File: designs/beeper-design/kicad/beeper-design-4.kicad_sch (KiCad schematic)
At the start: 37 parts, among them J1 TC2030-IDC-NL, J6 10103594-0001LF, U1 DA14705-00000HZ2, U2 AT25FF321A-UUN-T, U7 TPD4S012DRYR

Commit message: another export
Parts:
- removed C1: 22u, beeper-design:Pkg0603, symbol C86295
- removed C10: 2.2u, beeper-design:Pkg0201_37, symbol C335106_24
- removed C11: 2.2u, beeper-design:Pkg0201_29, symbol C335106_19
- removed C12: 2.2u, beeper-design:Pkg0201_48, symbol C335106_30
- removed C13: 2.2u, beeper-design:Pkg0201_51, symbol C335106_33
- removed C2: 22u, beeper-design:Pkg0603_1, symbol C86295_1
- removed C3: 22u, beeper-design:Pkg0603_2, symbol C86295_2
- removed C36: 2.2u, beeper-design:Pkg0201_49, symbol C335106_31
- removed C4: 47u, beeper-design:Pkg0805, symbol my_capacitor
- removed C49: 2.2u, beeper-design:Pkg0201_4, symbol C335106_1
- removed C5: 2.2u, beeper-design:Pkg0201_24, symbol C335106_14
- removed C50: 2.2u, beeper-design:Pkg0201_25, symbol C335106_15
- removed C6: 47u, beeper-design:Pkg0805_1, symbol my_capacitor_1
- removed C7: 2.2u, beeper-design:Pkg0201_50, symbol C335106_32
- removed C8: 2.2u, beeper-design:Pkg0201_6, symbol C335106_2
- removed C9: 2.2u, beeper-design:Pkg0201_22, symbol C335106_12
- removed J1: TC2030-IDC-NL, beeper-design:TC2030_IDC_NL_FOOTPRINT, symbol component_1
- removed J6: 10103594-0001LF, beeper-design:AMPHENOL_10103594_0001LF, symbol AMPHENOL_10103594_0001LF
- removed L1: 470n, beeper-design:Pkg0201_1, symbol my_inductor_3
- removed L2: 470n, beeper-design:Pkg0201_14, symbol my_inductor_1
- removed L3: 470n, beeper-design:Pkg0201_13, symbol my_inductor
- removed L4: 470n, beeper-design:Pkg0201_36, symbol my_inductor_2
- removed R1: 0R, beeper-design:Pkg0201_44, symbol my_resistor_11
- removed R18: 100K, beeper-design:Pkg0201_38, symbol my_resistor_8
- removed TP10, TP11, TP12, TP5, TP6, TP7, TP8, TP9: (no value), beeper-design:SMD_TESTPT, symbol smd_testpoint_cmp
- removed U1: DA14705-00000HZ2, beeper-design:LP, symbol DA14705
- removed U17: (no value), beeper-design:Pkg_2450AT18D0100_STD_R_1, symbol Sym2450AT18D0100001E
- removed U2: AT25FF321A-UUN-T, beeper-design:WLCSP_12, symbol AT25FF321A_UUN_T
- removed U7: TPD4S012DRYR, beeper-design:SON_6_L1_5_W1_0_P0_50_BL, symbol C96506
- removed XTAL1: XRCGB32M000F1H00R0, beeper-design:CRYSTAL_SMD_4P_L2_0_W1_6_BL_1, symbol C880116
- added C26: 2.2u, beeper-design:Pkg0201_42, symbol C335106_27
- added C27: 2.2u, beeper-design:Pkg0201_4, symbol C335106_2
- added C28: 2.2u, beeper-design:Pkg0201_47, symbol C335106_31
- added C29: 2.2u, beeper-design:Pkg0201_30, symbol C335106_20
- added C30: 2.2u, beeper-design:Pkg0201_16, symbol C335106_12
- added C31: 2.2u, beeper-design:Pkg0201_29, symbol C335106_19
- added C32: 2.2u, beeper-design:Pkg0201_17, symbol C335106_13
- added C37: 2.2u, beeper-design:Pkg0201_45, symbol C335106_29
- added C38: 2.2u, beeper-design:Pkg0201_3, symbol C335106_1
- added C39: 2.2u, beeper-design:Pkg0201_1, symbol C335106_36
- added C42: 2.2u, beeper-design:Pkg0201_50, symbol C335106_34
- added C43: 2.2u, beeper-design:Pkg0201_9, symbol C335106_7
- added D1: HL-PCF-1617S39FU70GH203BC-A, beeper-design:LP_5, symbol C513368
- added R10: 0R, beeper-design:Pkg0201_52, symbol my_resistor_12
- added R12, R13: 8K2, beeper-design:Pkg0201_36, symbol my_resistor_7
- added R14, R15: 8K2, beeper-design:Pkg0201_20, symbol my_resistor_3
- added R9: 0R, beeper-design:Pkg0201_43, symbol my_resistor_11
- added TP3, TP4: (no value), beeper-design:SMD_TESTPT, symbol smd_testpoint_cmp
- added U14, U15, U16: EVPBB4A9B000, beeper-design:LP_2, symbol C140848
- added U4: DA7212-01UM2, beeper-design:LP_3, symbol component_1
- added U9: LSM6DSOXTR, beeper-design:LP_1, symbol LSM6DSOXTR
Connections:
- net GND: now also C26.1, C27.1, C28.1, C29.1, C30.1, C31.1, C32.1, C37.1, C38.1, C39.1, C42.1, C43.1, U14.B, U14.B1, U15.B, U15.B1, U16.B, U16.B1, U4.B10 (GND_A), U4.B2 (GND_CP), U9.7 (GND)
- net VDD1P8: now also C42.2, C43.2, R14.2, R15.2, U9.5 (VDDIO), U9.8 (VDD)
- net VDD3P0: now also C26.2, C32.2, U4.B14 (VDD_MIC), U4.D10 (VDD_IO)
- net VLED: now also D1.2
- net board-io_qsen-i3c_scl: now also R10.1, R15.1, U9.13 (SCL)
- net board-io_rgb_b: now also D1.4
- net board-io_rgb_g: now also D1.3
- net board-io_rgb_r: now also D1.1
- net codec-i2c-net_scl: now also R13.1, U4.D8 (SCL)
- net codec-i2c-net_sda: now also R12.1, U4.C9 (SDA)
- net mcu_mcu-button0_gpio: now also U14.A, U14.A1
- net mcu_mcu-button1_gpio: now also U15.A, U15.A1
- net mcu_mcu-button2_gpio: now also U16.A, U16.A1
- net mcu_q-spi_cs: now also U9.12 (CS)
- net mcu_q-spi_sck: now also R10.2
- net mcu_q-spi_sdi: now also U9.1 (SDO_SA0)
- net mcu_q-spi_sdo: now also R9.2
- new net: C39.2, U4.B8 (VREF)
- new net: C27.2, U4.D12 (VDIG)
- new net: C31.2, U4.A7 (DACREF)
- new net: C38.2, U4.A17 (MICBIAS2)
- new net: C30.2, U4.A9 (VMID)
- new net MICBIAS1: C37.2, U4.A15 (MICBIAS1)
- new net SP_N: TP4.p, U4.A13 (SP_N)
- new net SP_P: TP3.p, U4.B12 (SP_P)
- new net VDD1P8P: C28.2, R12.2, R13.2, U4.B6 (VDD_A)
- new net VDDSYS: C29.2, U4.A11 (VDD_SP)
- new net board-io_qsen-i3c_sda: R14.1, R9.1, U9.14 (SDA)
- new net codec-pdm-net_clk: U4.C17 (MIC1_P)
- new net codec-pdm-net_data: U4.B16 (MIC1_N)
- no-connect marks 1 -> 7

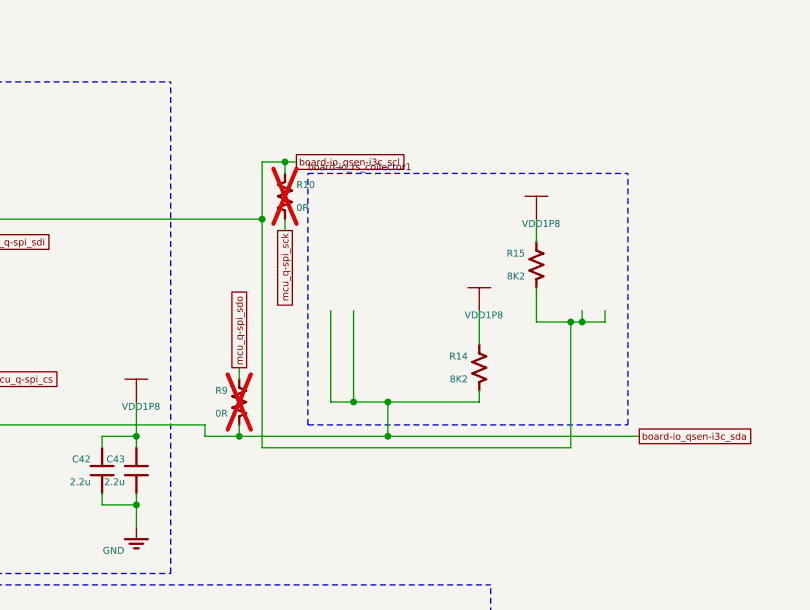
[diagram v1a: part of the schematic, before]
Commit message: crash with new usb connector
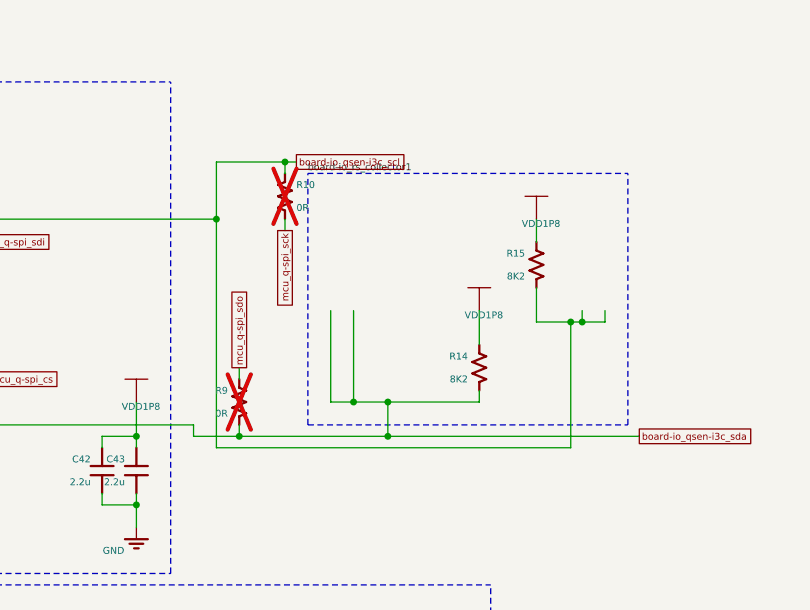
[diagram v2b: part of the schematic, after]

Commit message: new export
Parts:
- removed C26: 2.2u, beeper-design:Pkg0201_42, symbol C335106_27
- removed C27: 2.2u, beeper-design:Pkg0201_4, symbol C335106_2
- removed C28: 2.2u, beeper-design:Pkg0201_47, symbol C335106_31
- removed C29: 2.2u, beeper-design:Pkg0201_30, symbol C335106_20
- removed C30: 2.2u, beeper-design:Pkg0201_16, symbol C335106_12
- removed C31: 2.2u, beeper-design:Pkg0201_29, symbol C335106_19
- removed C32: 2.2u, beeper-design:Pkg0201_17, symbol C335106_13
- removed C37: 2.2u, beeper-design:Pkg0201_45, symbol C335106_29
- removed C38: 2.2u, beeper-design:Pkg0201_3, symbol C335106_1
- removed C39: 2.2u, beeper-design:Pkg0201_1, symbol C335106_36
- removed C42: 2.2u, beeper-design:Pkg0201_50, symbol C335106_34
- removed C43: 2.2u, beeper-design:Pkg0201_9, symbol C335106_7
- removed R14, R15: 8K2, beeper-design:Pkg0201_20, symbol my_resistor_3
- removed R9: 0R, beeper-design:Pkg0201_43, symbol my_resistor_11
- removed U4: DA7212-01UM2, beeper-design:LP_3, symbol component_1
- added C26: 2.2u, beeper-design:Pkg0201_34, symbol C335106_21
- added C27: 2.2u, beeper-design:Pkg0201_53, symbol C335106_33
- added C28: 2.2u, beeper-design:Pkg0201_42, symbol C335106_26
- added C29: 2.2u, beeper-design:Pkg0201_24, symbol C335106_15
- added C30: 2.2u, beeper-design:Pkg0201_8, symbol C335106_6
- added C31: 2.2u, beeper-design:Pkg0201_21, symbol C335106_13
- added C32: 2.2u, beeper-design:Pkg0201_11, symbol C335106_8
- added C37: 2.2u, beeper-design:Pkg0201_39, symbol C335106_24
- added C38: 2.2u, beeper-design:Pkg0201_51, symbol C335106_32
- added C39: 2.2u, beeper-design:Pkg0201_47, symbol C335106_28
- added C42: 2.2u, beeper-design:Pkg0201_43, symbol C335106_27
- added C43: 2.2u, beeper-design:Pkg0201_3, symbol C335106_1
- added R14, R15: 8K2, beeper-design:Pkg0201_14, symbol my_resistor_2
- added R9: 0R, beeper-design:Pkg0201_35, symbol my_resistor_9
- added U4: DA7212-01UM2, beeper-design:LP_3, symbol component_2
- R10: footprint beeper-design:Pkg0201_52 -> beeper-design:Pkg0201_44
- R12, R13: footprint beeper-design:Pkg0201_36 -> beeper-design:Pkg0201_29
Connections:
- net GND: now also C26.1, C27.1, C28.1, C29.1, C30.1, C31.1, C32.1, C37.1, C38.1, C39.1, C42.1, C43.1, U4.B10 (GND_A), U4.B2 (GND_CP)
- net MICBIAS1: now also C37.2, U4.A15 (MICBIAS1)
- net SP_N: now also U4.A13 (SP_N)
- net SP_P: now also U4.B12 (SP_P)
- net VDD1P8: now also C42.2, C43.2, R14.2, R15.2
- net VDD1P8P: now also C28.2, U4.B6 (VDD_A)
- net VDD3P0: now also C26.2, C32.2, U4.B14 (VDD_MIC), U4.D10 (VDD_IO)
- net VDDSYS: now also C29.2, U4.A11 (VDD_SP)
- net board-io_qsen-i3c_scl: now also R15.1
- net board-io_qsen-i3c_sda: now also R14.1, R9.1
- net codec-i2c-net_scl: now also U4.D8 (SCL)
- net codec-i2c-net_sda: now also U4.C9 (SDA)
- net codec-pdm-net_clk: now also U4.C17 (MIC1_P)
- net codec-pdm-net_data: now also U4.B16 (MIC1_N)
- net mcu_q-spi_sdo: now also R9.2
- new net: C38.2, U4.A17 (MICBIAS2)
- new net: C27.2, U4.D12 (VDIG)
- new net: C31.2, U4.A7 (DACREF)
- new net: C39.2, U4.B8 (VREF)
- new net: C30.2, U4.A9 (VMID)

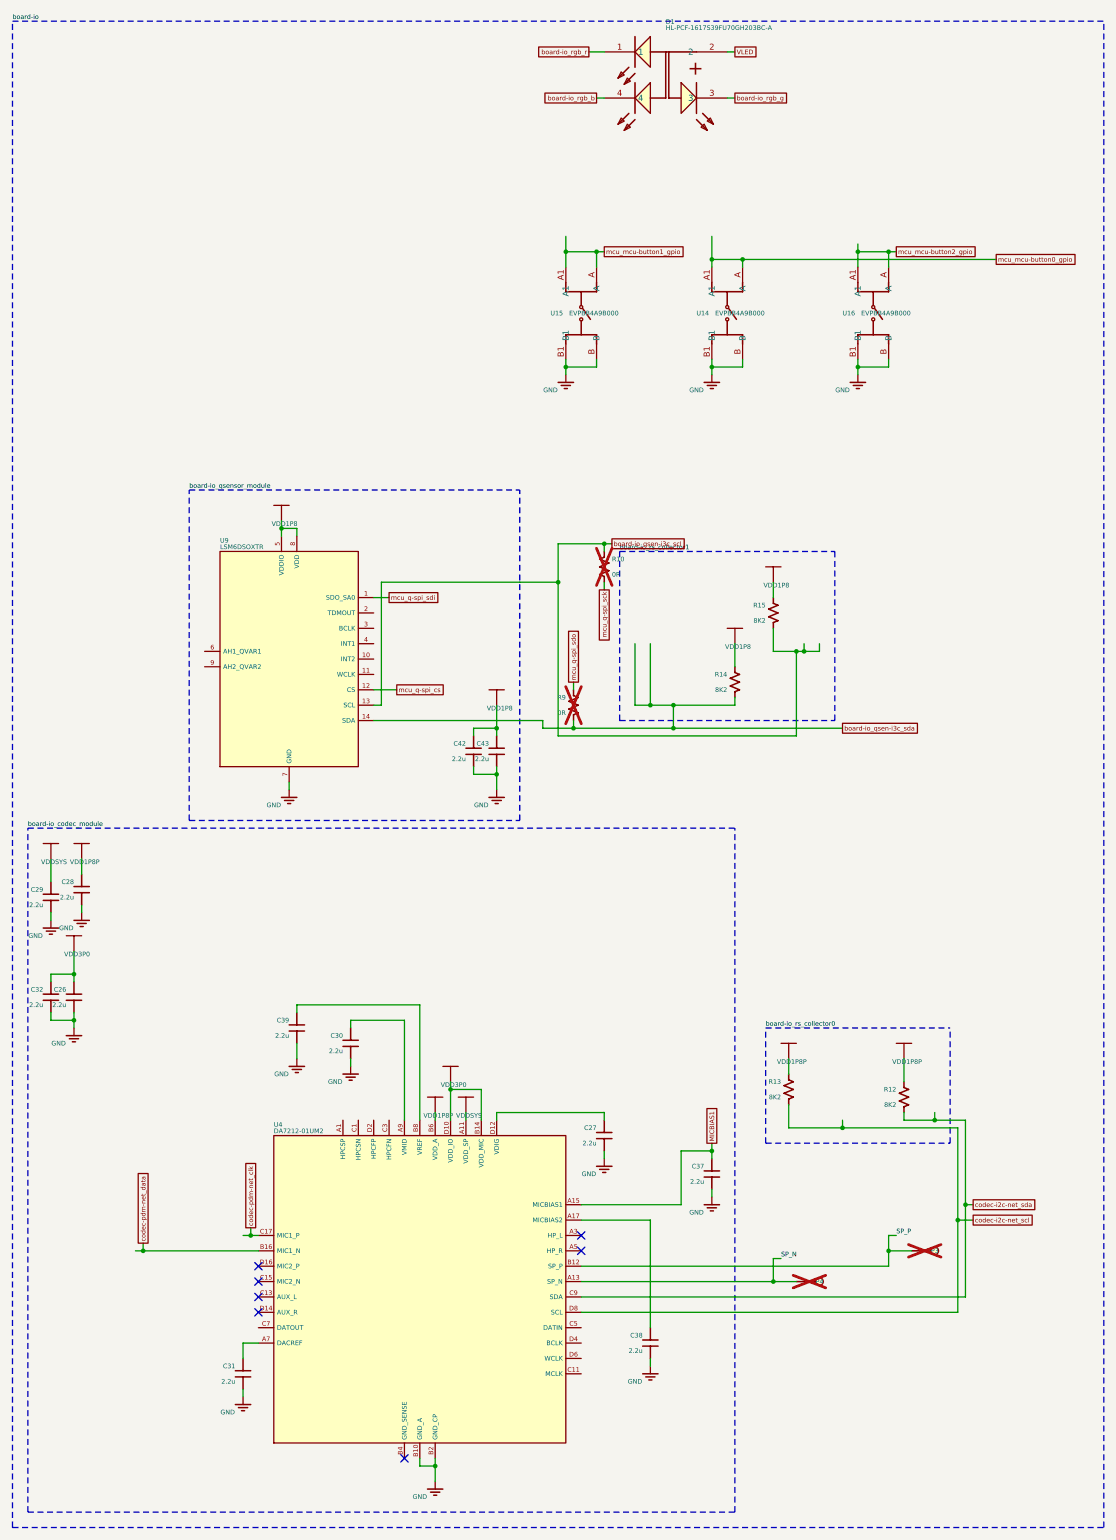
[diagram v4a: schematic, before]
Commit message: exported, yet XTALM32p keeps disappearing
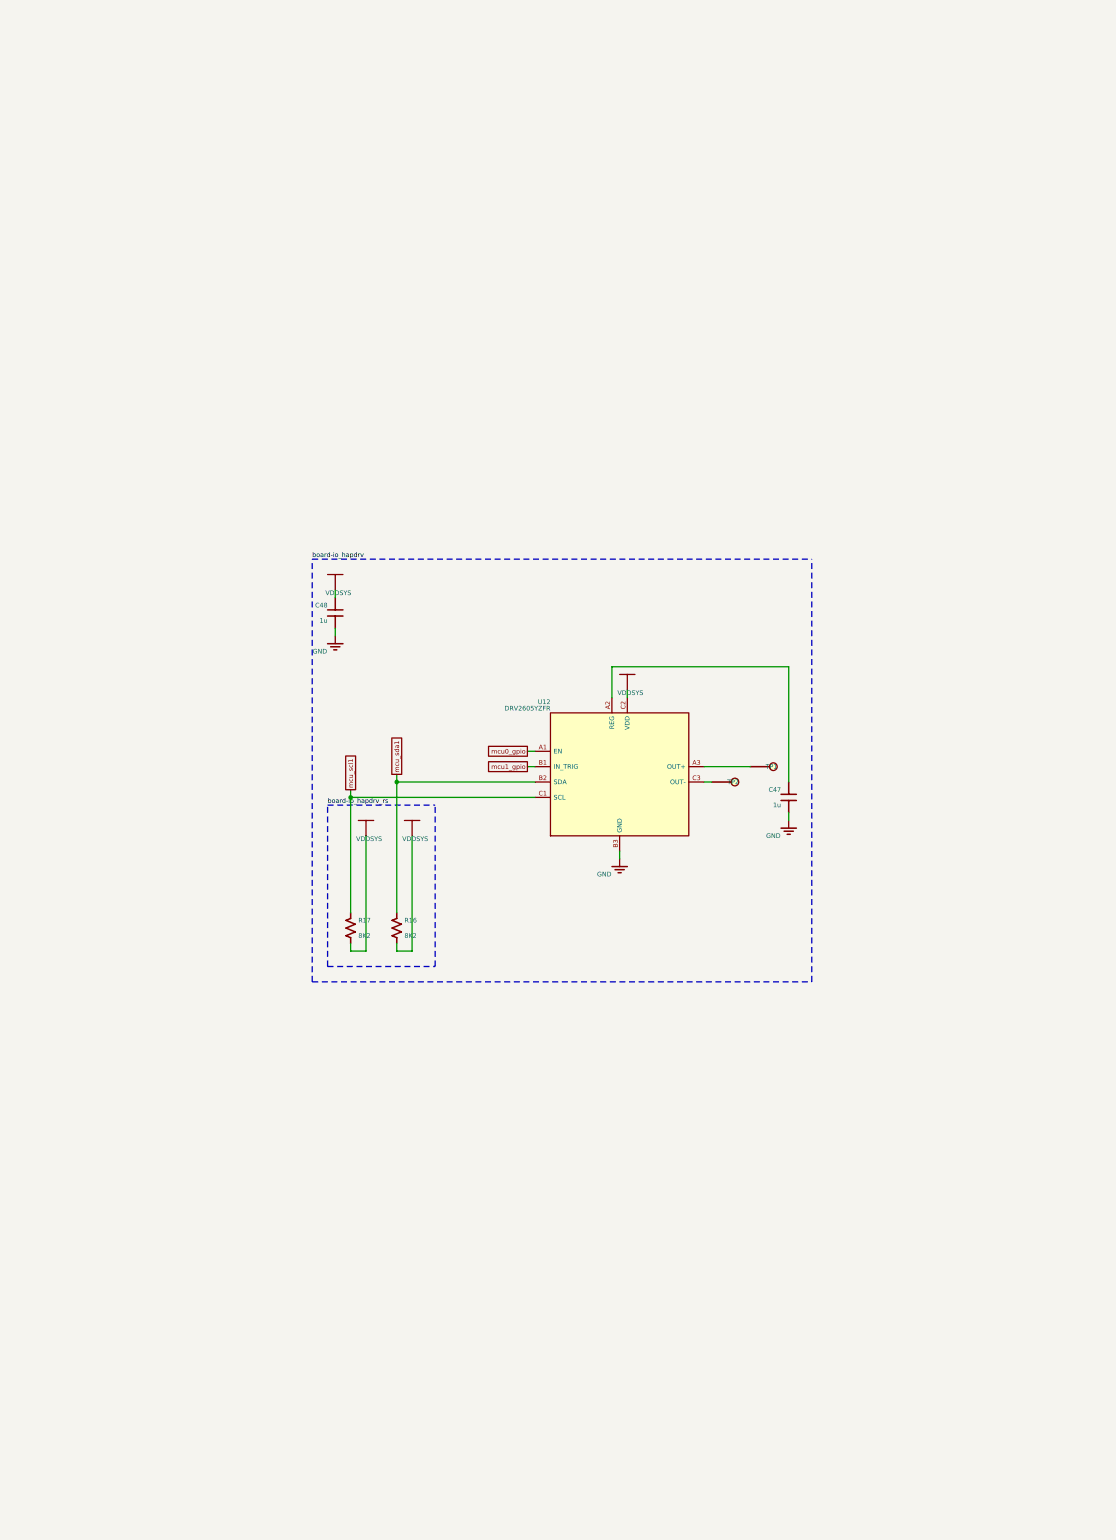
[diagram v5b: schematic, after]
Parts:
- removed C26: 2.2u, beeper-design:Pkg0201_34, symbol C335106_21
- removed C27: 2.2u, beeper-design:Pkg0201_53, symbol C335106_33
- removed C28: 2.2u, beeper-design:Pkg0201_42, symbol C335106_26
- removed C29: 2.2u, beeper-design:Pkg0201_24, symbol C335106_15
- removed C30: 2.2u, beeper-design:Pkg0201_8, symbol C335106_6
- removed C31: 2.2u, beeper-design:Pkg0201_21, symbol C335106_13
- removed C32: 2.2u, beeper-design:Pkg0201_11, symbol C335106_8
- removed C37: 2.2u, beeper-design:Pkg0201_39, symbol C335106_24
- removed C38: 2.2u, beeper-design:Pkg0201_51, symbol C335106_32
- removed C39: 2.2u, beeper-design:Pkg0201_47, symbol C335106_28
- removed C42: 2.2u, beeper-design:Pkg0201_43, symbol C335106_27
- removed C43: 2.2u, beeper-design:Pkg0201_3, symbol C335106_1
- removed D1: HL-PCF-1617S39FU70GH203BC-A, beeper-design:LP_5, symbol C513368
- removed R10: 0R, beeper-design:Pkg0201_44, symbol my_resistor_12
- removed R12, R13: 8K2, beeper-design:Pkg0201_29, symbol my_resistor_7
- removed R14, R15: 8K2, beeper-design:Pkg0201_14, symbol my_resistor_2
- removed R9: 0R, beeper-design:Pkg0201_35, symbol my_resistor_9
- removed TP3, TP4: (no value), beeper-design:SMD_TESTPT, symbol smd_testpoint_cmp
- removed U14, U15, U16: EVPBB4A9B000, beeper-design:LP_2, symbol C140848
- removed U4: DA7212-01UM2, beeper-design:LP_3, symbol component_2
- removed U9: LSM6DSOXTR, beeper-design:LP_1, symbol LSM6DSOXTR
- added C47: 1u, beeper-design:Pkg0201_26, symbol my_capacitor_14
- added C48: 1u, beeper-design:Pkg0201_33, symbol my_capacitor_18
- added R16, R17: 8K2, beeper-design:Pkg0201_40, symbol my_resistor_13
- added TP1, TP2: (no value), beeper-design:SMD_TESTPT, symbol smd_testpoint_cmp
- added U12: DRV2605YZFR, beeper-design:LP_7, symbol DRV2605YZFR
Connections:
- net GND: now also C47.1, C48.1, U12.B3 (GND)
- net VDDSYS: now also C48.2, R16.2, R17.2, U12.C2 (VDD)
- new net: TP2.p, U12.C3 (OUT-)
- new net: TP1.p, U12.A3 (OUT+)
- new net: C47.2, U12.A2 (REG)
- new net mcu0_gpio: U12.A1 (EN)
- new net mcu1_gpio: U12.B1 (IN_TRIG)
- new net mcu_scl1: R17.1, U12.C1 (SCL)
- new net mcu_sda1: R16.1, U12.B2 (SDA)
- no-connect marks 7 -> 0

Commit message: fixed up pours, keepout regions
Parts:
- removed C47: 1u, beeper-design:Pkg0201_26, symbol my_capacitor_14
- removed C48: 1u, beeper-design:Pkg0201_33, symbol my_capacitor_18
- removed R16, R17: 8K2, beeper-design:Pkg0201_40, symbol my_resistor_13
- added C47: 1u, beeper-design:Pkg0201_40, symbol my_capacitor_20
- added C48: 1u, beeper-design:Pkg0201_47, symbol my_capacitor_24
- added R16, R17: 8K2, beeper-design:Pkg0201_6, symbol my_resistor_1
- U12: footprint beeper-design:LP_7 -> beeper-design:LP_2
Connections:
- net GND: now also C47.1, C48.1
- net VDDSYS: now also C48.2, R16.2, R17.2
- net mcu_scl1: now also R17.1
- net mcu_sda1: now also R16.1
- net at U12.A2 (REG): now also C47.2

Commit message: exported to Kicad, fixed Kicad, exported gerbers
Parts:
- removed C47: 1u, beeper-design:Pkg0201_40, symbol my_capacitor_20
- removed C48: 1u, beeper-design:Pkg0201_47, symbol my_capacitor_24
- removed R16, R17: 8K2, beeper-design:Pkg0201_6, symbol my_resistor_1
- added C47: 1u, beeper-design:Pkg0201_7, symbol my_capacitor_3
- added C48: 1u, beeper-design:Pkg0201_14, symbol my_capacitor_7
- added R16, R17: 8K2, beeper-design:Pkg0201_21, symbol my_resistor_3
- U12: footprint beeper-design:LP_2 -> beeper-design:LP_7
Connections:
- net GND: now also C47.1, C48.1
- net VDDSYS: now also C48.2, R16.2, R17.2
- net mcu_scl1: now also R17.1
- net mcu_sda1: now also R16.1
- net at U12.A2 (REG): now also C47.2
